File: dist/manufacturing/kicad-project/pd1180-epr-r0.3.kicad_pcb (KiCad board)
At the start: 4 copper layers, 85.9 x 85.9 mm, 269 parts, among them J1 J1, J10 J10, J2 J2, J3 J3, J6 J6, J7 J7, J9 J9, Q1 Q1, Q10 Q10, Q11 Q11, Q12 Q12, Q13 Q13, Q14 Q14, Q15 Q15, Q16 Q16, Q17 Q17, Q18 Q18, Q19 Q19, Q2 Q2, Q20 Q20, Q21 Q21, Q22 Q22, Q23 Q23, Q24 Q24, Q25 Q25, Q3 Q3, Q4 Q4, Q5 Q5, Q6 Q6, Q7 Q7, Q8 Q8, Q9 Q9, SW1 SW1, U1 TPD4S480RUKR, U10 SN74LVC1G08DBVR, U11 SN74LVC1G08DBVR, U12 TL431AIDBZR, U13 TLV3201AIDBVR, U14 TLV3201AIDBVR, U15 UCC27511DBVR, U16 STM32G0B1CBT6, U17 W25Q32JVSSIQ, U18 AS5047P-ATSM, U19 TCAN332DR, U2 TPS26750SRSMR, U20 MAX3485EESA+T, U21 MAX3232ESE+T, U22 LMR36510ADDAR, U23 LM66100DCKR, U24 LM66100DCKR, U3 M24512-RMN6TP, U4 SN74LVC1G08DBVR, U5 LMR36510ADDAR, U6 TPS26631RGER, U7 TMC5160A-TA-T, U8 74LVC1G157GW,125, U9 74LVC1G157GW,125, Y1 Y1

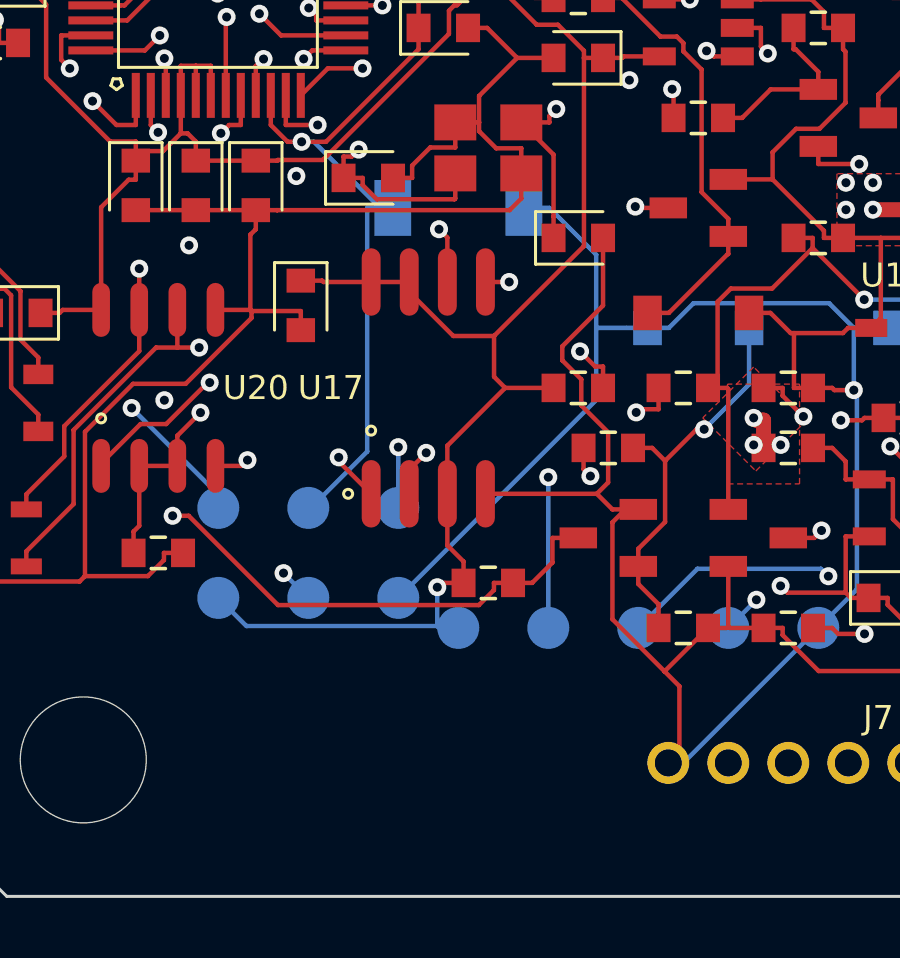
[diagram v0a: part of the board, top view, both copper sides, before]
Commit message: Fix schematic style and top-side reset switch
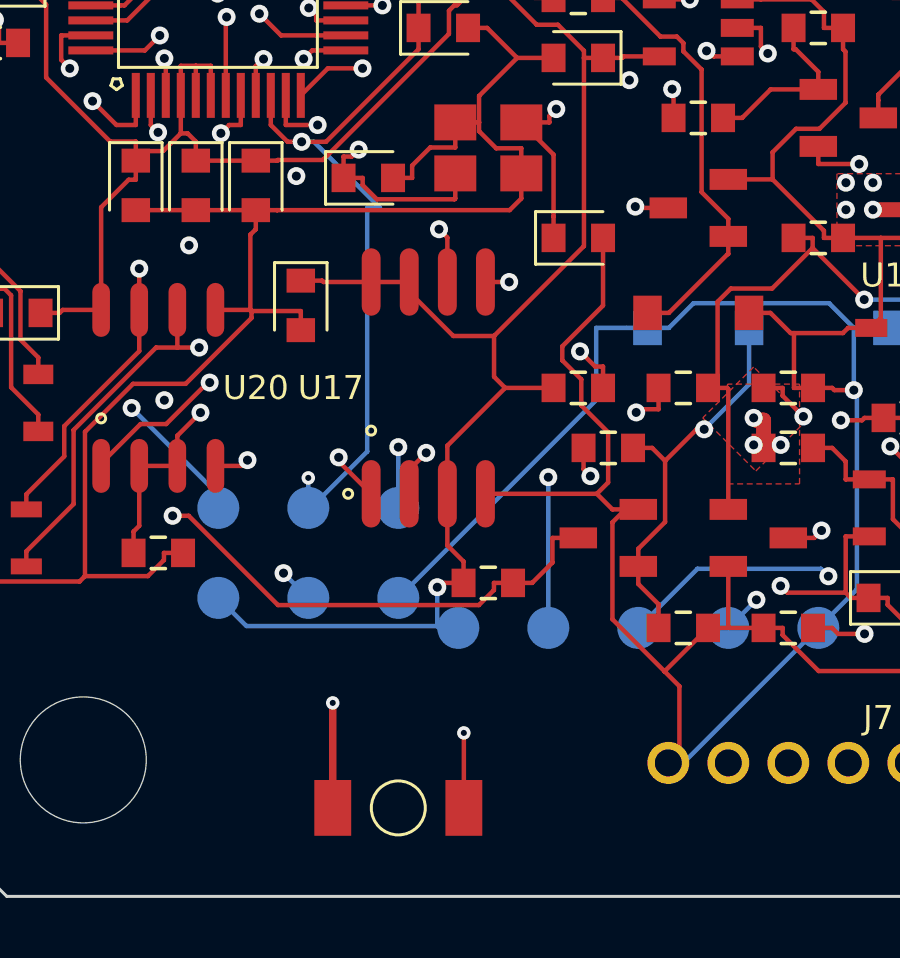
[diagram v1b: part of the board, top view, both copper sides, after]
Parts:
- SW1: moved to F.Cu
- moved SW1 20.1 mm to (86.0, 140.0), turned to 0 degrees
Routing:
- net NRST: track 25.4 -> 38.4 mm, vias 1 -> 3
- net GND: track 989.8 -> 987.8 mm, vias 14 -> 15
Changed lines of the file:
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@@
 		(embedded_fonts no)
 	)
+	(footprint "TS-1088-AR02016"
+		(layer "F.Cu")
+		(at 86 140)
+		(property "Reference" "SW1"
+			(at 0 3 0)
+			(layer "B.SilkS")
+			(hide yes)
+			(effects
+				(font
+					(size 1.27 1.27)
+					(thickness 0.15)
+				)
+				(justify mirror)
+			)
+		)
+		(property "Value" "SW1"
+			(at 0 -3 0)
+			(layer "B.Fab")
+			(hide yes)
+			(effects
+				(font
+					(size 1.27 1.27)
+					(thickness 0.15)
+				)
+				(justify mirror)
+			)
+		)
+		(property "Datasheet" ""
+			(at 0 0 0)
+			(layer "B.Fab")
+			(hide yes)
+			(effects
+				(font
+					(size 1.27 1.27)
+					(thickness 0.15)
+				)
+				(justify mirror)
+			)
+		)
+		(property "Description" ""
+			(at 0 0 0)
+			(layer "B.Fab")
+			(hide yes)
+			(effects
+				(font
+					(size 1.27 1.27)
+					(thickness 0.15)
+				)
+				(justify mirror)
+			)
+		)
+		(property "Supplier Part Number" "C720477"
+			(at 0 0 0)
+			(layer "B.Fab")
+			(hide yes)
+			(effects
+				(font
+					(size 1.27 1.27)
+					(thickness 0.15)
+				)
+				(justify mirror)
+			)
+		)
+		(property "MPN" "TS-1088-AR02016"
+			(at 0 0 0)
+			(layer "B.Fab")
+			(hide yes)
+			(effects
+				(font
+					(size 1.27 1.27)
+					(thickness 0.15)
+				)
+				(justify mirror)
+			)
+		)
+		(duplicate_pad_numbers_are_jumpers no)
+		(fp_circle
+			(center 0 0)
+			(end 0.899922 0)
+			(stroke
+				(width 0.1)
+				(type default)
+			)
+			(fill no)
+			(layer "F.SilkS")
+		)
+		(fp_poly
+			(pts
+				(xy 3.049905 1.70001) (xy -3.049905 1.70001) (xy -3.049905 -1.699984) (xy 3.049905 -1.699984) (xy 3.049905 1.70001)
+			)
+			(stroke
+				(width 0.05)
+				(type default)
+			)
+			(fill no)
+			(layer "F.CrtYd")
+		)
+		(fp_line
+			(start -2.026209 -1.541196)
+			(end 2.026209 -1.541196)
+			(stroke
+				(width 0.1)
+				(type default)
+			)
+			(layer "F.Fab")
+		)
+		(fp_line
+			(start -2.026209 -1.110132)
+			(end -2.026209 -1.541196)
+			(stroke
+				(width 0.1)
+				(type default)
+			)
+			(layer "F.Fab")
+		)
+		(fp_line
+			(start -2.026209 1.541196)
+			(end -2.026209 1.110132)
+			(stroke
+				(width 0.1)
+				(type default)
+			)
+			(layer "F.Fab")
+		)
+		(fp_line
+			(start -2.026209 1.541196)
+			(end 2.026209 1.541196)
+			(stroke
+				(width 0.1)
+				(type default)
+			)
+			(layer "F.Fab")
+		)
+		(fp_line
+			(start 2.026209 -1.541196)
+			(end 2.026209 -1.110132)
+			(stroke
+				(width 0.1)
+				(type default)
+			)
+			(layer "F.Fab")
+		)
+		(fp_line
+			(start 2.026209 1.541196)
+			(end 2.026209 1.110132)
+			(stroke
+				(width 0.1)
+				(type default)
+			)
+			(layer "F.Fab")
+		)
+		(pad "1" smd rect
+			(at 2.184908 0 180)
+			(size 1.229995 1.859991)
+			(layers "F.Cu" "F.Mask" "F.Paste")
+			(net "NRST")
+		)
+		(pad "2" smd rect
+			(at -2.184908 0 180)
+			(size 1.229995 1.859991)
+			(layers "F.Cu" "F.Mask" "F.Paste")
+			(net "GND")
+		)
+		(embedded_fonts no)
+		(model "https://modelcdn.tscircuit.com/easyeda_models/assets/C720477.step?uuid=2e35dca8e7854ed683469f8d54d1ef17&cachebust_origin="
+			(offset
+				(xyz -0 -0.0000127000000703 0)
+			)
+			(scale
+				(xyz 1 1 1)
+			)
+			(rotate
+				(xyz 0 0 -180)
+			)
+		)
+	)
 	(footprint "capacitor_cap0603"
 		(layer "F.Cu")
@@
 		)
 	)
-	(footprint "TS-1088-AR02016"
-		(layer "B.Cu")
-		(at 88 120 180)
-		(property "Reference" "SW1"
-			(at 0 -3 0)
-			(layer "F.SilkS")
-			(hide yes)
-			(effects
-				(font
-					(size 1.27 1.27)
-					(thickness 0.15)
-				)
-			)
-		)
-		(property "Value" "SW1"
-			(at 0 3 0)
-			(layer "F.Fab")
-			(hide yes)
-			(effects
-				(font
-					(size 1.27 1.27)
-					(thickness 0.15)
-				)
-			)
-		)
-		(property "Datasheet" ""
-			(at 0 0 0)
-			(layer "F.Fab")
-			(hide yes)
-			(effects
-				(font
-					(size 1.27 1.27)
-					(thickness 0.15)
-				)
-			)
-		)
-		(property "Description" ""
-			(at 0 0 0)
-			(layer "F.Fab")
-			(hide yes)
-			(effects
-				(font
-					(size 1.27 1.27)
-					(thickness 0.15)
-				)
-			)
-		)
-		(property "Supplier Part Number" "C720477"
-			(at 0 0 0)
-			(layer "F.Fab")
-			(hide yes)
-			(effects
-				(font
-					(size 1.27 1.27)
-					(thickness 0.15)
-				)
-			)
-		)
-		(property "MPN" "TS-1088-AR02016"
-			(at 0 0 0)
-			(layer "F.Fab")
-			(hide yes)
-			(effects
-				(font
-					(size 1.27 1.27)
-					(thickness 0.15)
-				)
-			)
-		)
-		(duplicate_pad_numbers_are_jumpers no)
-		(fp_circle
-			(center 0 0)
-			(end 0.899922 0)
-			(stroke
-				(width 0.1)
-				(type default)
-			)
-			(fill no)
-			(layer "B.SilkS")
-		)
-		(fp_poly
-			(pts
-				(xy 3.049905 -1.70001) (xy -3.049905 -1.70001) (xy -3.049905 1.699984) (xy 3.049905 1.699984) (xy 3.049905 -1.70001)
-			)
-			(stroke
-				(width 0.05)
-				(type default)
-			)
-			(fill no)
-			(layer "B.CrtYd")
-		)
-		(fp_line
-			(start 2.026209 1.541196)
-			(end 2.026209 1.110132)
-			(stroke
-				(width 0.1)
-				(type default)
-			)
-			(layer "B.Fab")
-		)
-		(fp_line
-			(start 2.026209 -1.541196)
-			(end 2.026209 -1.110132)
-			(stroke
-				(width 0.1)
-				(type default)
-			)
-			(layer "B.Fab")
-		)
-		(fp_line
-			(start -2.026209 1.541196)
-			(end 2.026209 1.541196)
-			(stroke
-				(width 0.1)
-				(type default)
-			)
-			(layer "B.Fab")
-		)
-		(fp_line
-			(start -2.026209 1.110132)
-			(end -2.026209 1.541196)
-			(stroke
-				(width 0.1)
-				(type default)
-			)
-			(layer "B.Fab")
-		)
-		(fp_line
-			(start -2.026209 -1.541196)
-			(end 2.026209 -1.541196)
-			(stroke
-				(width 0.1)
-				(type default)
-			)
-			(layer "B.Fab")
-		)
-		(fp_line
-			(start -2.026209 -1.541196)
-			(end -2.026209 -1.110132)
-			(stroke
-				(width 0.1)
-				(type default)
-			)
-			(layer "B.Fab")
-		)
-		(pad "1" smd rect
-			(at 2.184908 0)
-			(size 1.229995 1.859991)
-			(layers "B.Cu" "B.Mask" "B.Paste")
-			(net "NRST")
-		)
-		(pad "2" smd rect
-			(at -2.184908 0)
-			(size 1.229995 1.859991)
-			(layers "B.Cu" "B.Mask" "B.Paste")
-			(net "GND")
-		)
-		(embedded_fonts no)
-		(model "https://modelcdn.tscircuit.com/easyeda_models/assets/C720477.step?uuid=2e35dca8e7854ed683469f8d54d1ef17&cachebust_origin="
-			(offset
-				(xyz -0 -0.0000127000000703 0)
-			)
-			(scale
-				(xyz 1 1 1)
-			)
-			(rotate
-				(xyz 0 0 -180)
-			)
-		)
-	)
 	(footprint "resistor_res0603"
 		(layer "B.Cu")
@@
 	)
 	(segment
+		(start 88.184908 140)
+		(end 88.1849 137.5)
+		(width 0.15)
+		(layer "F.Cu")
+		(net "NRST")
+	)
+	(segment
 		(start 82.7785 117.7964)
 		(end 83.5903 117.7964)
@@
 	)
 	(via
+		(at 83 129)
+		(size 0.45)
+		(drill 0.2)
+		(layers "F.Cu" "B.Cu")
+		(net "NRST")
+	)
+	(via
 		(at 82.7785 117.7964)
 		(size 0.6)
@@
 		(net "NRST")
 	)
+	(via
+		(at 88.1849 137.5)
+		(size 0.45)
+		(drill 0.2)
+		(layers "F.Cu" "B.Cu")
+		(net "NRST")
+	)
 	(segment
 		(start 83 130)
@@
 	)
 	(segment
-		(start 85.8151 120)
-		(end 85.3893 120)
+		(start 83 129)
+		(end 83 130)
 		(width 0.15)
 		(layer "B.Cu")
@@
 	)
 	(segment
+		(start 88.1849 137.5)
+		(end 83 129)
+		(width 0.15)
+		(layer "In1.Cu")
+		(net "NRST")
+	)
+	(segment
 		(start 96.325 97)
 		(end 96.325 97.9267)
@@
 	)
 	(segment
+		(start 83.815092 140)
+		(end 83.8151 136.5)
+		(width 0.25)
+		(layer "F.Cu")
+		(net "GND")
+	)
+	(segment
 		(start 110.3208 72.2265)
 		(end 112.9193 74.825)
@@
 	)
 	(via
+		(at 83.8151 136.5)
+		(size 0.45)
+		(drill 0.2)
+		(layers "F.Cu" "B.Cu")
+		(net "GND")
+	)
+	(via
 		(at 136.7 107.2)
 		(size 0.45)
@@
 	)
 	(segment
-		(start 92.5972 121.5606)
-		(end 91.0366 120)
-		(width 0.15)
-		(layer "B.Cu")
-		(net "GND")
-	)
-	(segment
 		(start 129.175 118)
 		(end 129.8117 118)
@@
 	)
 	(segment
-		(start 90.1849 120)
-		(end 91.0366 120)
-		(width 0.15)
-		(layer "B.Cu")
-		(net "GND")
-	)
-	(segment
 		(start 117.9668 131.6035)
 		(end 119.9348 131.6035)
@@
 		(width 0.15)
 		(layer "B.Cu")
-		(net "GND")
-	)
-	(segment
-		(start 92.5972 124)
-		(end 92.5972 121.5606)
-		(width 0.15)
-		(layer "B.Cu")

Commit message: Use one USB-C port for PD and data
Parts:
- removed J10: J10, USB4105-GF-A
- removed R105, R106: 5.1kΩ, resistor_res0603
- R107: value 100kΩ -> 1MΩ
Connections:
- net USB_DATA_VBUS_SENSE renamed USB_VBUS_SENSE
- J1 pad 11: (no net) -> USB_DP_CONN
- J1 pad 12: (no net) -> USB_DM_CONN
- J1 pad 13: (no net) -> USB_DP_CONN
- J1 pad 14: (no net) -> USB_DM_CONN
- R107 pad 1: USB_DATA_VBUS -> USB_VBUS
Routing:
- net GND: track 987.8 -> 951.7 mm, vias 15 -> 19
- net USB_DATA_VBUS: track 24.0 -> 0.00 mm
- net USB_VBUS: track 128.9 -> 151.3 mm, vias 28 -> 29
- net USB_DATA_CC1: track 18.6 -> 0.00 mm, vias 2 -> 0
- net USB_DATA_CC2: track 15.2 -> 0.00 mm, vias 2 -> 0
- net USB_DM_CONN: track 24.8 -> 18.3 mm
- net USB_DP_CONN: track 24.9 -> 19.3 mm, vias 2 -> 3
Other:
- board text removed: "J10 USB DATA"

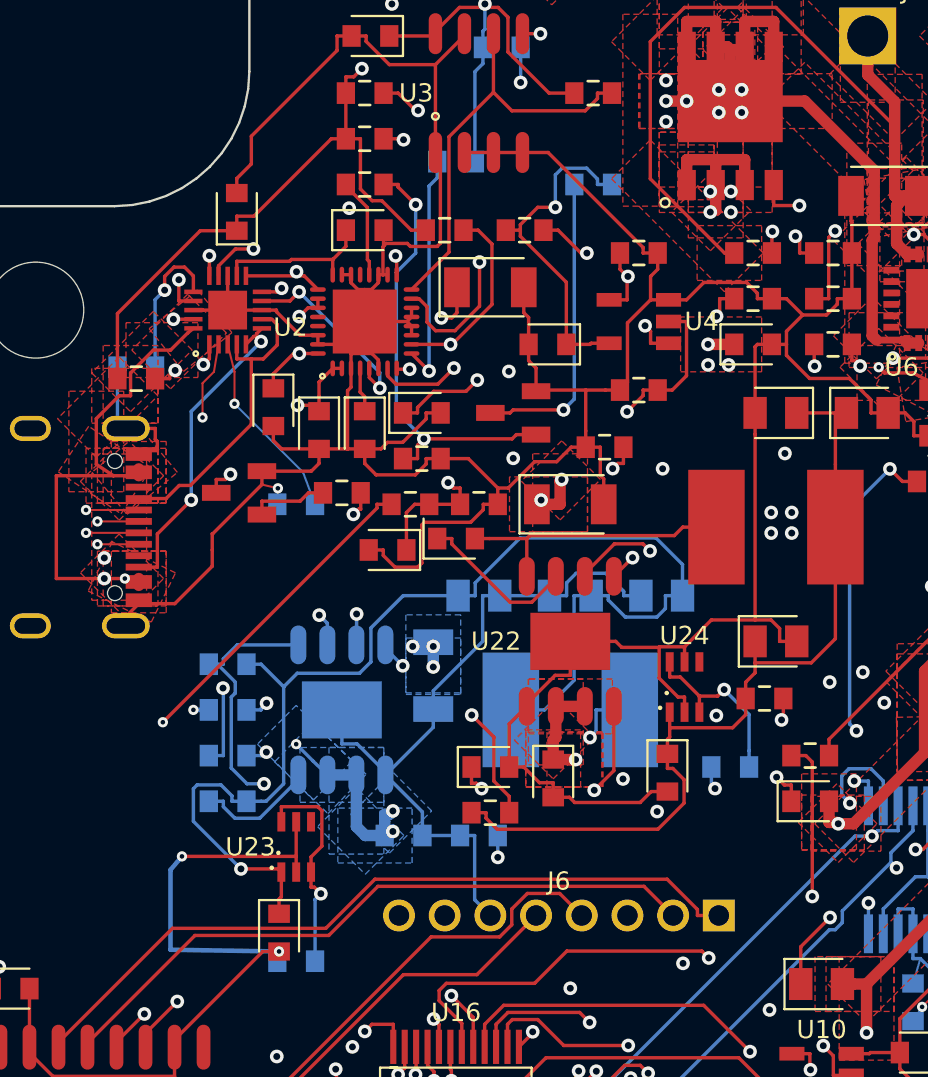
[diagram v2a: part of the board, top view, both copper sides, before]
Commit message: fix: finalize single-port EPR controller
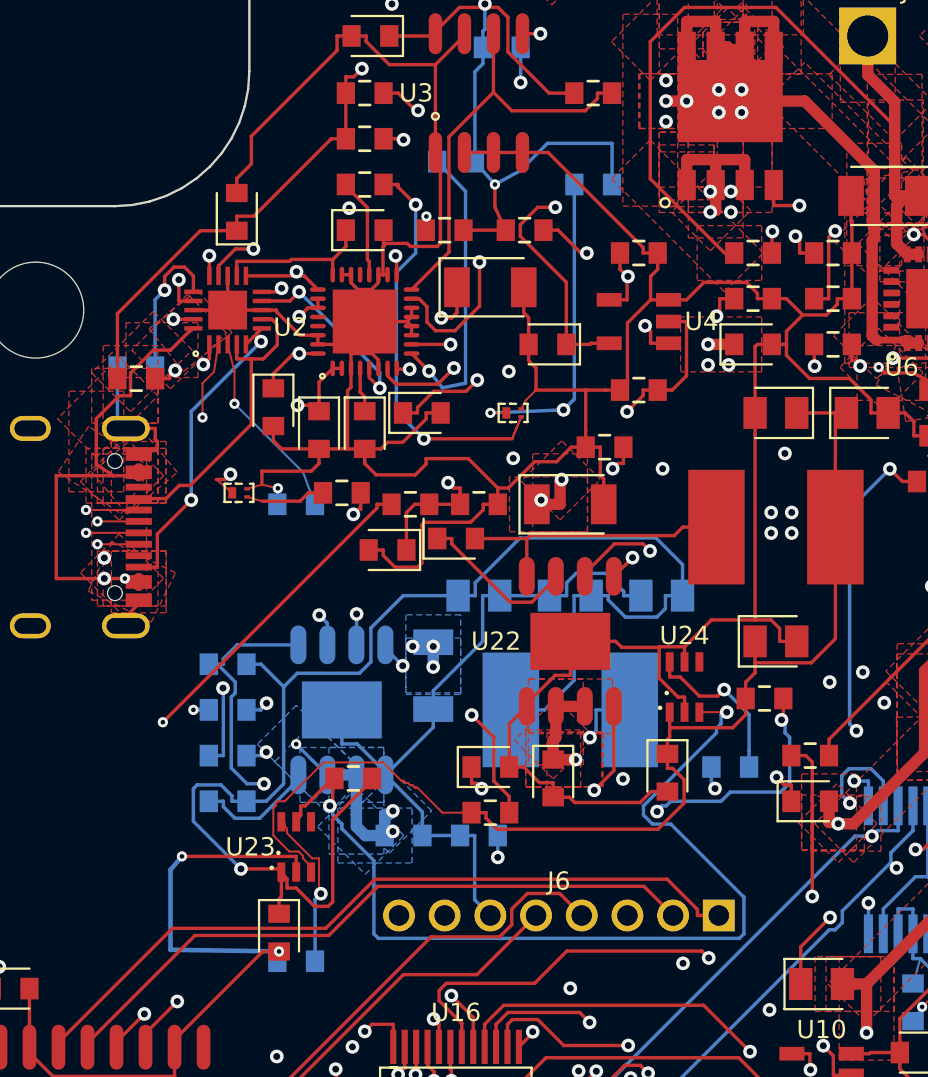
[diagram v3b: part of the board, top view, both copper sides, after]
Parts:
- removed R10: 100kΩ, resistor_res0603
- added R111: 10kΩ, resistor_res0603, F.Cu at (75.5, 96.0)
- C2: value 100nF -> 1uF
- Q2, Q3: footprint MMBT5551LT1G -> CSD17484F4
- R108: value 100kΩ -> 47kΩ
- R11, R13: value 10kΩ -> 100kΩ
- R12: value 10kΩ -> 0Ω
- R9: value 100kΩ -> 0Ω
- turned Q2 to 180 degrees
- turned Q3 to 180 degrees
- turned R8 to 180 degrees
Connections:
- J1 pad 10: (no net) -> unconnected-(J1-SBU1-Pad10)
- J1 pad 16: (no net) -> unconnected-(J1-SBU2-Pad16)
- R11 pad 1: V3V3 -> PD_3V3
- R13 pad 1: V3V3 -> PD_3V3
- U18 pad 10: (no net) -> unconnected-(U18-U-Pad10)
- U18 pad 8: (no net) -> unconnected-(U18-W-Pad8)
- U18 pad 9: (no net) -> unconnected-(U18-V-Pad9)
- U19 pad 5: (no net) -> unconnected-(U19-NC1-Pad5)
- U19 pad 8: (no net) -> unconnected-(U19-NC2-Pad8)
- U2 pad 21: (no net) -> unconnected-(U2-NC-Pad21)
- U2 pad 28: (no net) -> unconnected-(U2-PP5V1-Pad28)
- U2 pad 29: (no net) -> unconnected-(U2-PP5V2-Pad29)
- U21 pad 7: (no net) -> unconnected-(U21-T2OUT-Pad7)
- U21 pad 9: (no net) -> unconnected-(U21-R2OUT-Pad9)
- U23 pad 3: V3V3 -> V3V3_MOTOR
- U23 pad 4: (no net) -> unconnected-(U23-NC-Pad4)
- U23 pad 5: GND -> LOGIC_OR_PRIORITY
- U24 pad 3: V3V3 -> LOGIC_OR_PRIORITY
- U24 pad 4: (no net) -> unconnected-(U24-NC-Pad4)
- U6 pad 11: (no net) -> unconnected-(U6-MODE-Pad11)
- U6 pad 19: (no net) -> unconnected-(U6-N_C6-Pad19)
- U6 pad 20: (no net) -> unconnected-(U6-N_C5-Pad20)
- U6 pad 21: (no net) -> unconnected-(U6-N_C4-Pad21)
- U6 pad 22: (no net) -> unconnected-(U6-N_C3-Pad22)
- U6 pad 23: (no net) -> unconnected-(U6-N_C2-Pad23)
- U6 pad 24: (no net) -> unconnected-(U6-N_C1-Pad24)
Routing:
- net LOGIC_OR_PRIORITY: track 0.00 -> 41.5 mm, vias 0 -> 2
- net V3V3_MOTOR: track 37.6 -> 51.8 mm
- net V3V3_USB: track 55.3 -> 64.6 mm
- net V3V3: track 473.0 -> 464.7 mm
- net GND: track 951.7 -> 943.5 mm
- net PD_3V3: track 73.2 -> 79.6 mm, vias 4 -> 5
- net PD_SCL: track 48.2 -> 51.1 mm
- net MOTOR_LOGIC_PG: track 16.4 -> 17.4 mm, vias 4 -> 3
- net PD_LEVEL_BASE: track 19.5 -> 18.9 mm
- net PD_PATH_N: track 25.5 -> 26.2 mm, vias 2 -> 3
- net PD_IRQ_N: vias 2 -> 3
